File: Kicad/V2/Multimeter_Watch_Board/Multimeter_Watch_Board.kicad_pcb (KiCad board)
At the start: 4 copper layers, 46 x 42 mm, 52 parts, among them J1 S3B-PH-K-S(LF)(SN), J2 S3B-PH-K-S(LF)(SN), J3 S3B-PH-K-S(LF)(SN), J6 51281-1294, J7 Conn_01x11_Female, J8 Conn_01x11_Female, Q1 A03400A N-MOS, U1 PCF85163-SO08, U2 AD8592, Y1 32kHz

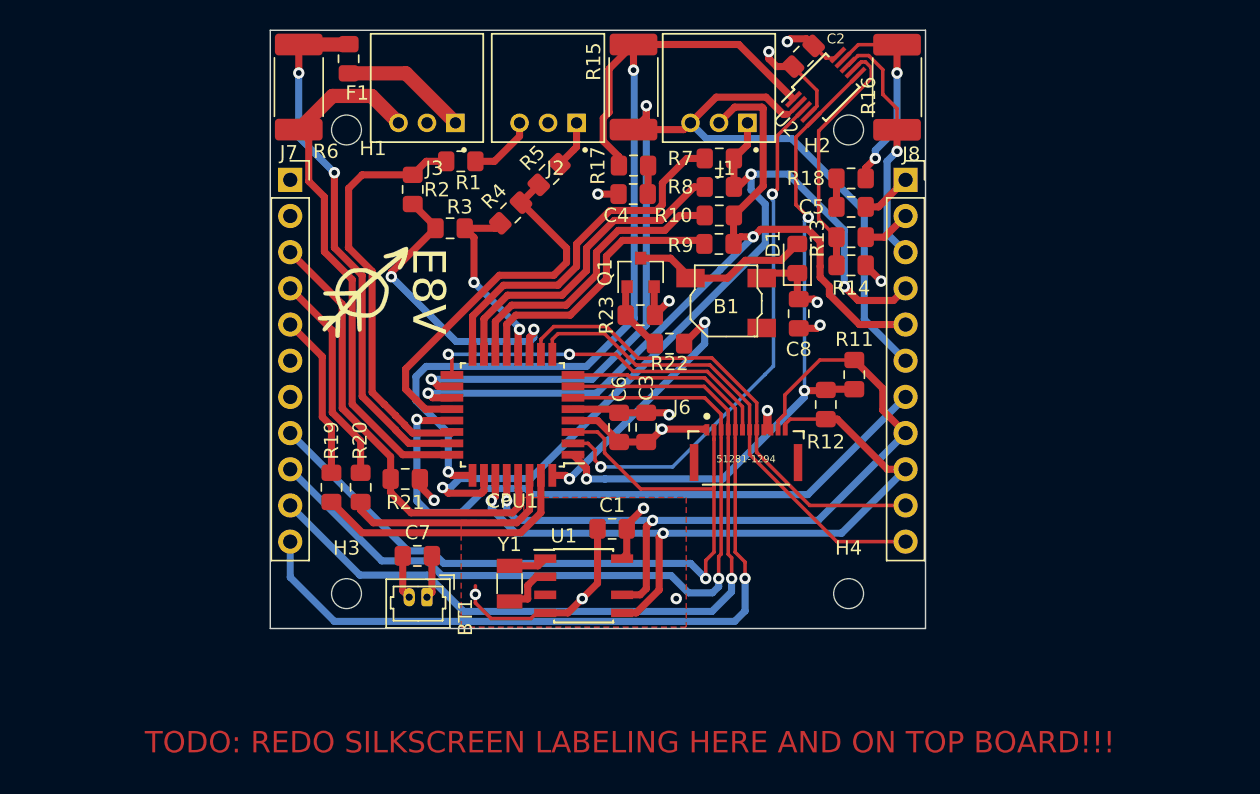
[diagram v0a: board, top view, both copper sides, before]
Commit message: drc update and fixes to bottom board
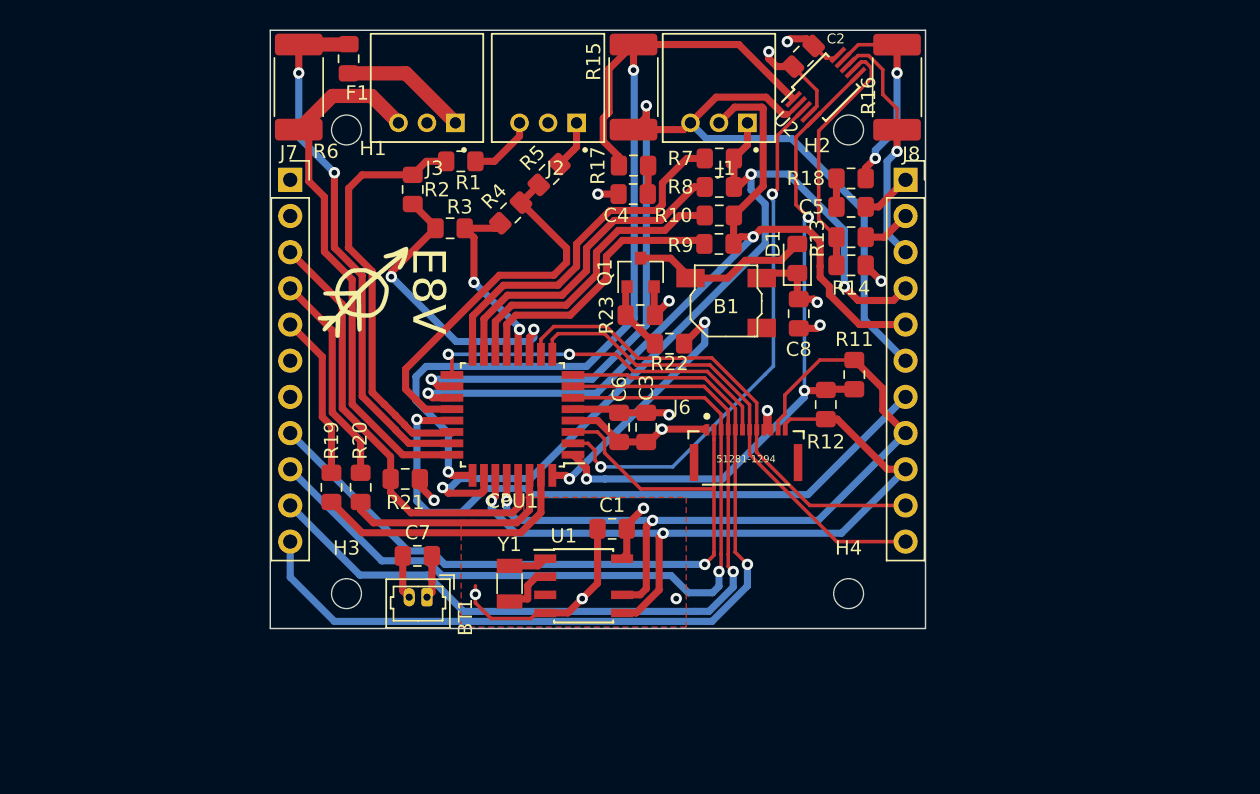
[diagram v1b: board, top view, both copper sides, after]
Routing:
- net /PE4: track 56.4 -> 55.0 mm
- net /PB7: track 62.9 -> 62.1 mm
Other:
- net class Default: clearance 0.2 -> 0.15
- rule trace_clearance: 0.2 -> 0.15
- rule trace_min: 0.2 -> 0.15
- board text removed: "TODO: REDO SILKSCREEN LABELING HERE AND ON TOP BOARD!!!"
